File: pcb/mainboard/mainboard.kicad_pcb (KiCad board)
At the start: 10 copper layers, 165 x 121 mm, 629 parts, among them J1 CONN_PCIE_PWR_8PIN, J10 FAN_01, J11 XILINX_JTAG, J12 JUMPER_0402_SPDT, J13 JUMPER_0402_SPDT, J14 RJ45, J15 PMOD_HOST, J16 SMPM, J17 SMPM, J18 SMPM, J19 SMPM, J2 CONN_IBC_MGMT, J20 SMPM, J21 SMPM, J22 SMPM, J23 SMPM, J24 SMPM, J25 SMPM, J26 SMPM, J27 0826-1G1T-23-F, J28 SMPM, J29 SMPM, J3 CONN_01X03, J30 SMPM, J31 SMPM, J32 SMPM, J33 SMPM, J34 SMPM, J35 SMPM, J36 SMPM, J37 SMPM, J38 SMPM, J39 SMPM, J4 CONN_01X05, J40 SMPM, J41 SMPM, J42 SMPM, J43 SMPM, J44 SMPM, J45 SMPM, J46 SMPM, J47 SMPM, J48 CONN_01X10, J5 XILINX_JTAG, J6 CONN_SFP_HOST, J7 SFP_CAGE, J8 FAN_01, J9 CONN_01X03, K1 RELAY_TE_HF3_96, K2 RELAY_TE_HF3_96, K3 RELAY_TE_HF3_96, K4 RELAY_TE_HF3_96, M1 960-23-23-F-AB-0, SW1 SWITCH, SW2 SWITCH, U1 STM32L031C6U6, U10 MAX40026, U11 MAX40026, U12 MAX40026, U13 MAX40026, U14 MAX40026, U15 MAX40026, U16 MAX40026, U17 MAX40026, U18 MAX40026, U19 MAX40026, U2 MYMGK1R812ERSR, U20 MAX40026, U21 DAC60508, U22 DAC60508, U23 STM32H735-UFBGA176-25, U24 AT24MAC402, U25 ADM3101E_QFN, U26 LMR70503, U27 SIT9121AI-2BF-XXS200.000000G, U28 SIT9121AI-2BF-XXS156.250000G, U29 HMC675LP3E, U3 MYMGK00504ERSR, U30 SIT9121AI-2BF-XXS200.000000G, U31 ECS-1612MV-250-CN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

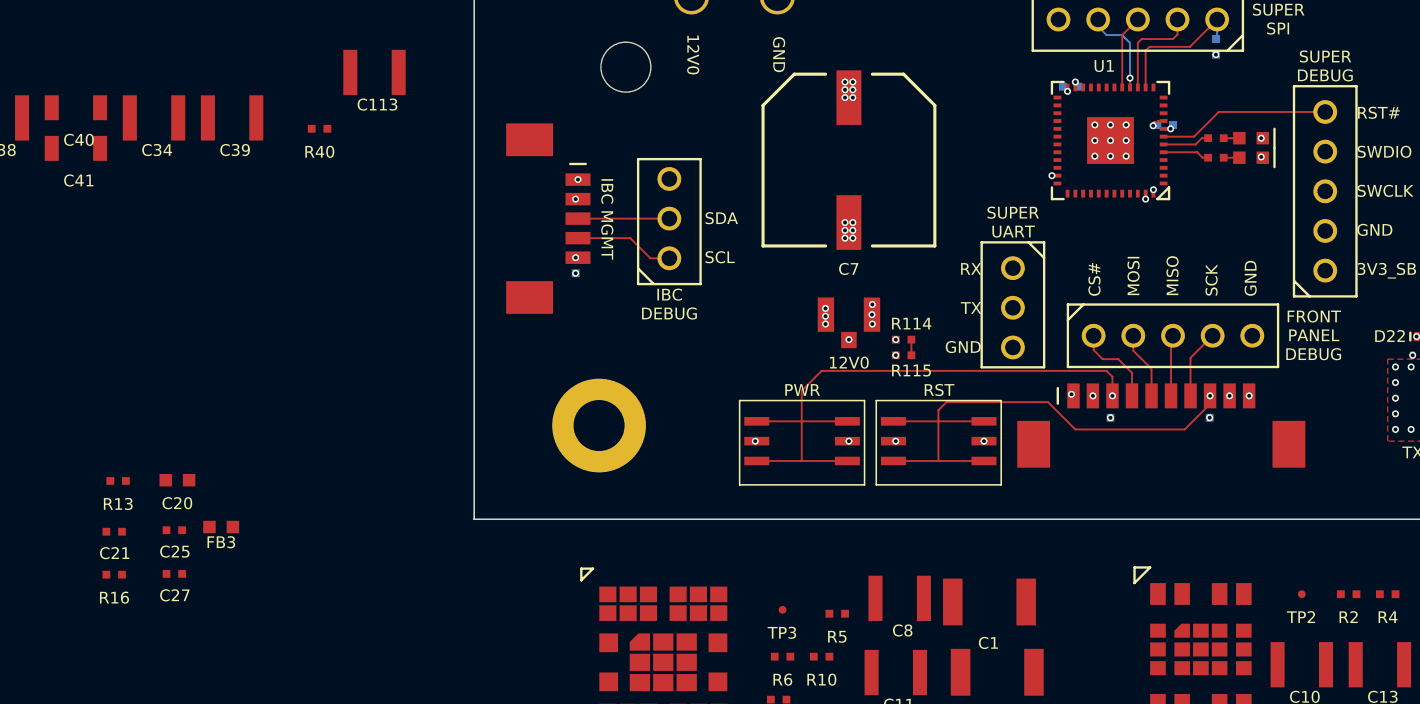
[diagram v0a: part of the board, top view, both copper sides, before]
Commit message: Initial power etc routing for supervisor
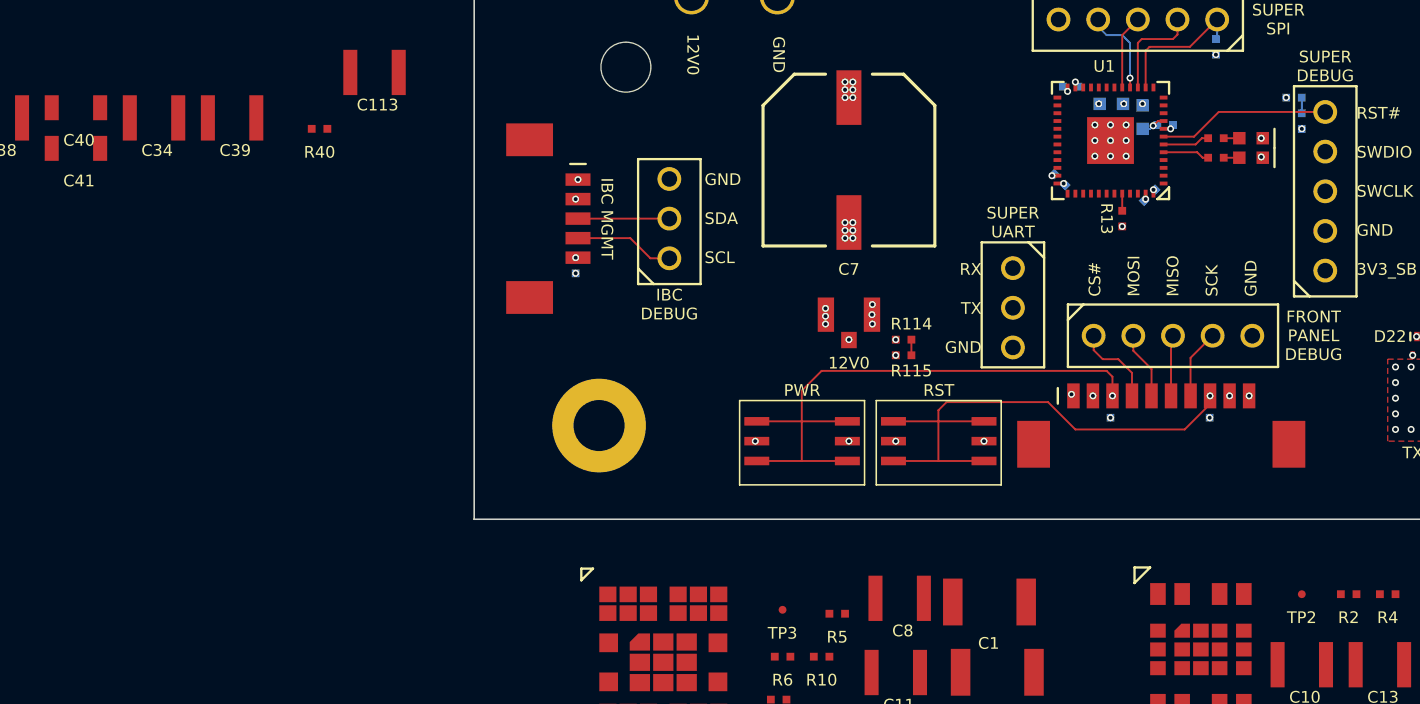
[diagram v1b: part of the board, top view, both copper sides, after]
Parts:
- C20, C21, C25, C27, FB3, R16: moved to B.Cu
- moved R16 81.5 mm to (167.5, 114.0)
- moved C21 80.5 mm to (168.0, 115.5), turned to -90 degrees
- moved C27 67.0 mm to (158.2, 120.2), turned to 45 degrees
- moved R13 66.5 mm to (156.5, 121.8), turned to -90 degrees
- moved FB3 64.6 mm to (157.8, 115.2), turned to 90 degrees
- moved C20 64.5 mm to (155.8, 114.4), turned to 180 degrees
- moved C25 61.0 mm to (152.5, 119.2), turned to 135 degrees
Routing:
- net /3V3_SB: track 266.0 -> 274.5 mm, vias 12 -> 16
- net /GND: track 2362.4 -> 2367.8 mm, vias 1336 -> 1339
- net /Power Supply/RST_N: track 11.0 -> 13.5 mm
- net /Power Supply/BOOT0: track 0.00 -> 1.10 mm
- net /Power Supply/A3V3_SUPER: track 0.80 -> 1.59 mm
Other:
- board text removed: "Management"

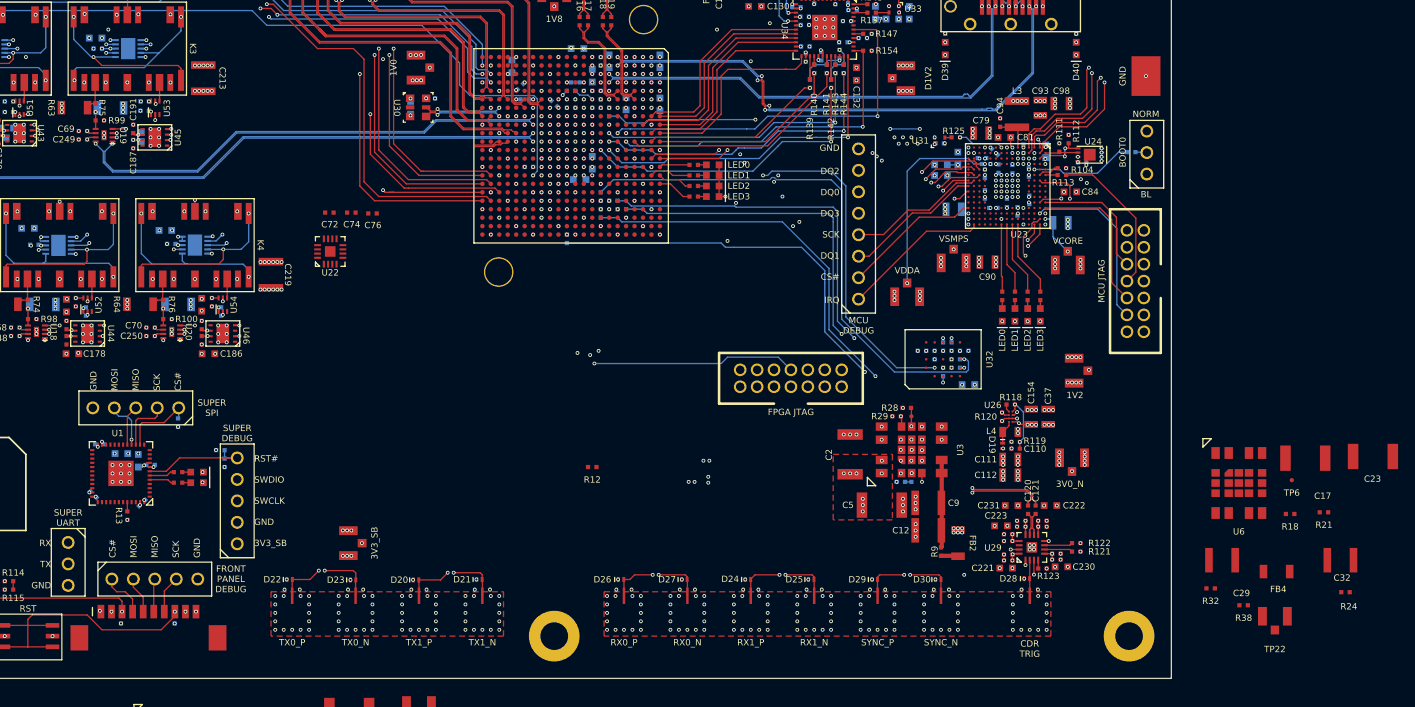
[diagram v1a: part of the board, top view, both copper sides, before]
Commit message: Initial layout of GTX_1V8 supply
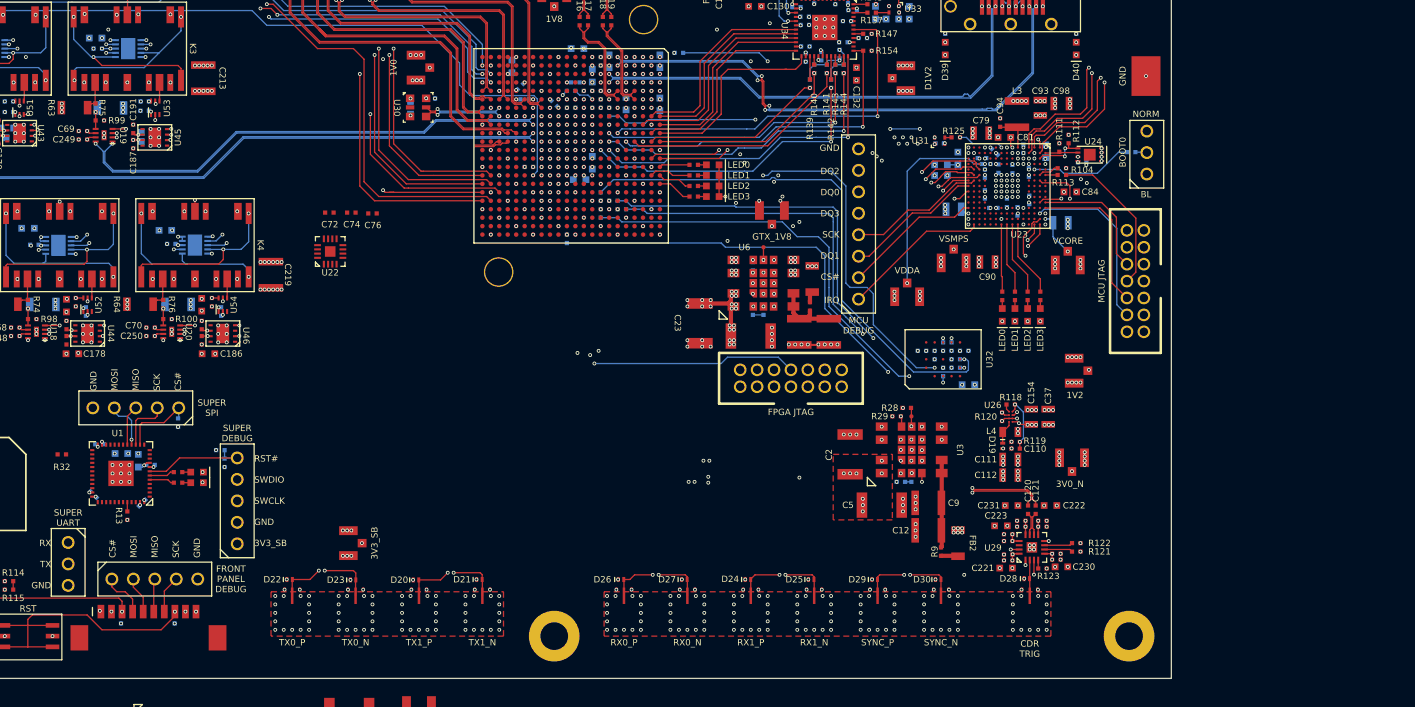
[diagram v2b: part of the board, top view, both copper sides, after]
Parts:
- R12, R18, R21, R38: moved to B.Cu
- moved R32 136.8 mm to (148.8, 114.5)
- moved C23 81.1 mm to (224.2, 99.0), turned to -90 degrees
- moved TP22 76.4 mm to (232.8, 85.8)
- moved R24 71.8 mm to (237.2, 97.0), turned to -90 degrees
- moved R21 71.6 mm to (230.5, 97.5), turned to -90 degrees
- moved R38 70.6 mm to (230.5, 92.2), turned to -90 degrees
- moved TP6 68.3 mm to (231.8, 90.0)
- moved C17 67.2 mm to (230.2, 100.5)
- moved R18 66.8 mm to (231.8, 97.5), turned to -90 degrees
- moved C32 66.3 mm to (239.5, 100.0), turned to -90 degrees
- moved FB4 64.9 mm to (237.5, 93.8), turned to 90 degrees
- moved U6 61.0 mm to (231.8, 94.2), turned to 90 degrees
- moved C29 56.8 mm to (236.0, 100.0), turned to -90 degrees
- moved R12 50.1 mm to (221.8, 67.0)
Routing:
- net /GND: track 2367.8 -> 2435.9 mm, vias 1339 -> 1385
- net /Power Supply/1V2_SENSE: track 15.7 -> 77.9 mm, vias 1 -> 3
- net /12V0: track 290.4 -> 314.6 mm, vias 64 -> 86
- net /FPGA Support/GTX_1V8: track 46.8 -> 59.7 mm, vias 2 -> 7
- net /Power Supply/GTX_1V8_RAW: track 0.00 -> 8.74 mm
- net /1V2: track 202.5 -> 204.1 mm, vias 22 -> 23
- net /Power Supply/GTX_1V8_PGOOD: track 0.00 -> 1.50 mm, vias 0 -> 1
- net /Management/FLASH_DQ3: track 52.8 -> 51.3 mm
- net /Management/FLASH_DQ2: track 53.3 -> 52.0 mm
- net /Management/FLASH_DQ0: track 64.9 -> 63.6 mm
- net Net-(FB4-Pad1): track 0.00 -> 1.31 mm
- net Net-(R18-Pad2): track 0.00 -> 1.25 mm
- net /Management/FLASH_CS_N: track 55.3 -> 54.7 mm
- net /Power Supply/GTX_1V8_EN: track 0.00 -> 0.05 mm, vias 0 -> 1
- net Net-(R18-Pad1): vias 0 -> 1
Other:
- board text added: "GTX_1V8"
- board text removed: "GTX_1V8 supply"

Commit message: More work in supervisor region
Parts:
- moved R40 45.7 mm to (150.8, 117.8)
- moved C40 21.0 mm to (109.2, 121.7)
- moved C41 21.0 mm to (109.2, 124.2)
- moved C38 21.0 mm to (104.2, 122.3)
- moved R32 14.0 mm to (161.2, 120.8)
- moved C113 5.32 mm to (110.8, 117.2)
- moved C34 5.30 mm to (99.5, 117.0)
- moved C39 5.30 mm to (104.5, 117.0)
- turned C27 to -135 degrees
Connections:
- U1 pad 11: /Power Supply/12V0_VMON -> /FPGA Support/FPGA_INIT
- U1 pad 13: /FPGA Support/FPGA_INIT -> /Power Supply/1V2_EN
- U1 pad 19: /Power Supply/1V2_EN -> /Power Supply/12V0_VMON
- U8 pad E21: /Management/FRONTPANEL_CS_N -> /Management/MCU_QSPI_SCK
- U8 pad E22: /Management/FRONTPANEL_MOSI -> /Management/MCU_QSPI_DQ1
- U8 pad F20: unconnected-(U8-PadF20) -> /Management/MCU_QSPI_DQ0
- U8 pad F21: unconnected-(U8-PadF21) -> /Management/MCU_QSPI_DQ3
- U8 pad G20: unconnected-(U8-PadG20) -> /Management/MCU_QSPI_DQ2
- U8 pad G22: /Management/FRONTPANEL_SCK -> /Management/FAN1_TACH
- U8 pad H22: /Management/FRONTPANEL_MISO -> /Management/MCU_QSPI_CS_N
- U8 pad J21: /Management/FAN1_TACH -> /Management/MCU_IRQ
- U8 pad K21: /Management/MCU_QSPI_SCK -> /Management/FRONTPANEL_MOSI
- U8 pad K22: /Management/MCU_QSPI_DQ2 -> /Management/FRONTPANEL_SCK
- U8 pad L20: /Management/MCU_QSPI_DQ0 -> unconnected-(U8-PadL20)
- U8 pad L21: /Management/MCU_QSPI_DQ3 -> /Management/FRONTPANEL_CS_N
- U8 pad M20: /Management/MCU_IRQ -> unconnected-(U8-PadM20)
- U8 pad M21: /Management/MCU_QSPI_CS_N -> unconnected-(U8-PadM21)
- U8 pad N22: /Management/MCU_QSPI_DQ1 -> /Management/FRONTPANEL_MISO
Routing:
- net /Management/FAN2_PWM: track 109.8 -> 199.9 mm, vias 1 -> 3
- net /Management/MCU_IRQ: track 17.5 -> 53.2 mm, vias 0 -> 1
- net /3V3: track 893.8 -> 928.7 mm, vias 157 -> 160
- net /FPGA Support/SFP_LED1: track 10.9 -> 45.6 mm, vias 2 -> 3
- net /FPGA Support/SFP_LED2: track 26.5 -> 61.0 mm, vias 2 -> 4
- net /Management/MCU_QSPI_DQ2: track 16.7 -> 51.1 mm, vias 2 -> 3
- net /Management/MCU_QSPI_CS_N: track 16.4 -> 49.0 mm, vias 0 -> 1
- net /Power Supply/SUPER_I2C_SCL: track 6.38 -> 38.3 mm, vias 0 -> 1
- net /Power Supply/12V0_VMON: track 1.00 -> 32.6 mm, vias 0 -> 4
- net /Management/MCU_QSPI_DQ0: track 16.3 -> 47.6 mm, vias 2 -> 3
- net /Management/MCU_QSPI_DQ3: track 19.5 -> 49.0 mm, vias 2 -> 3
- net /Management/SFP_RX_LOS: track 97.1 -> 126.4 mm, vias 3 -> 5
- net /Management/MCU_QSPI_DQ1: track 16.4 -> 45.5 mm, vias 0 -> 1
- net /Management/MCU_QSPI_SCK: track 16.3 -> 44.7 mm, vias 0 -> 1
- net /Power Supply/SUPER_I2C_SDA: track 5.85 -> 32.7 mm, vias 0 -> 1
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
